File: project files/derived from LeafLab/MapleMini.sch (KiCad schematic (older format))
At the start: 39 parts

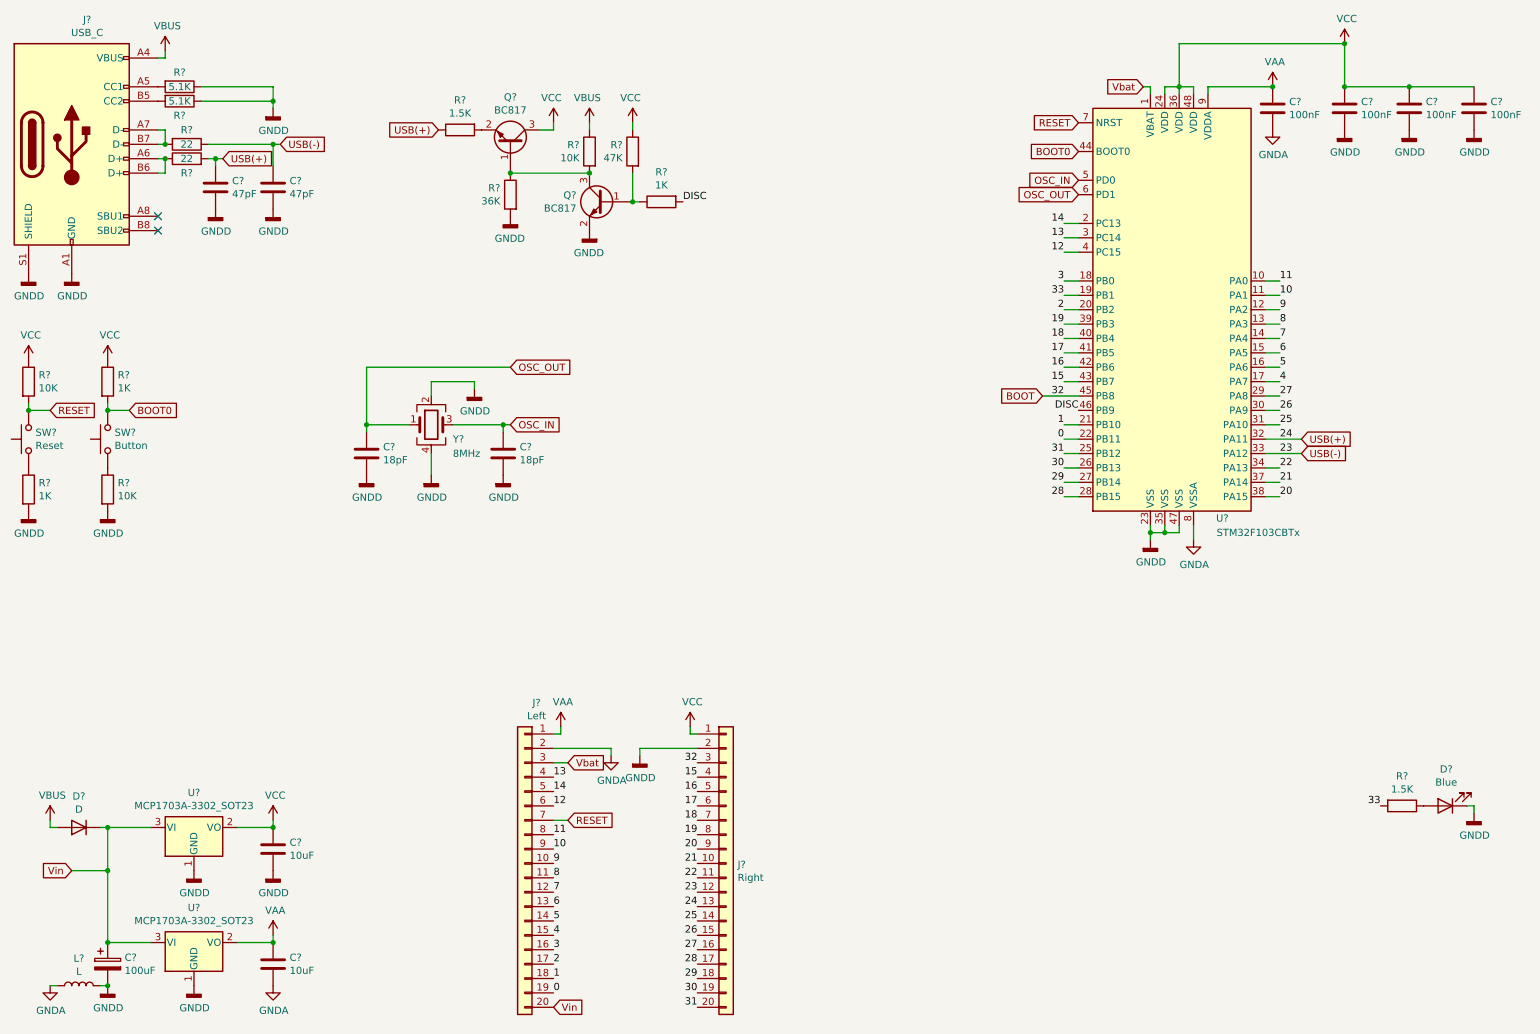
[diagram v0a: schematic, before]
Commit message: major re-arrangements
- Added references
- Added second schematic as derived from (supposengly) BAITE clone
- Renamed first design as LeafLabs-derived
- Added README.md
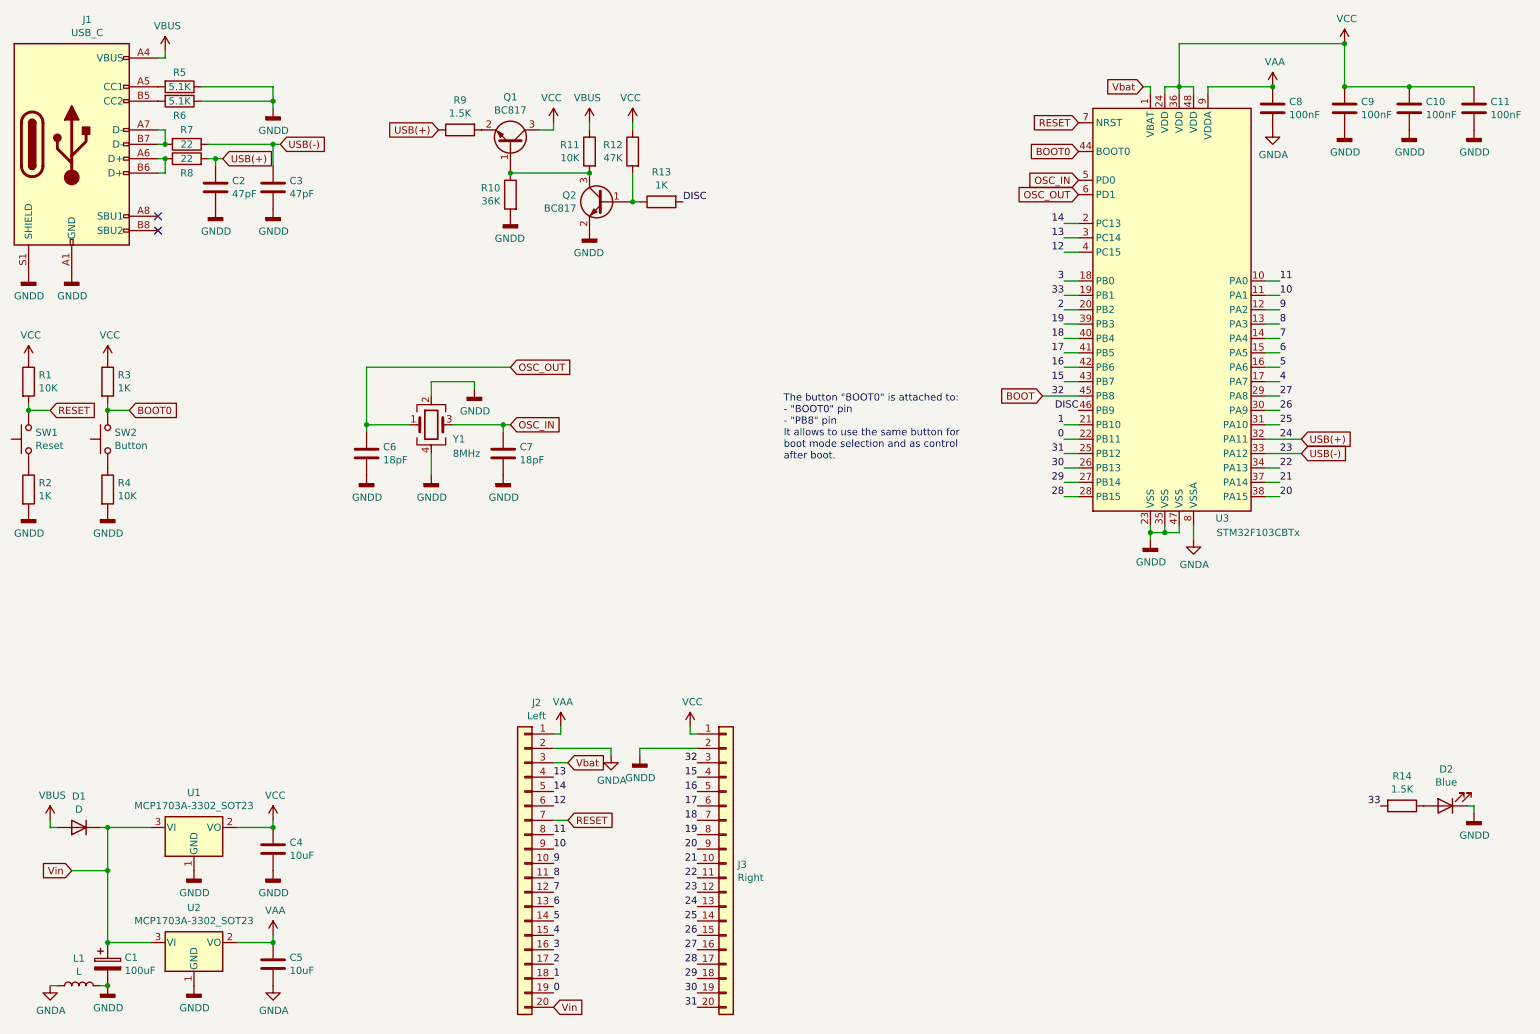
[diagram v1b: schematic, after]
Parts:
- C1, C10, C11, C2, C3, C4, C5, C6, C7, C8, C9: renamed from C?; footprint (none) -> Capacitor_SMD:C_0603_1608Metric
- D1: renamed from D?; footprint (none) -> Diode_SMD:D_SOD-323
- D2: renamed from D?; footprint (none) -> LED_SMD:LED_0805_2012Metric_Castellated
- J1: renamed from J?; footprint (none) -> Connector_USB:USB_C_Receptacle_Palconn_UTC16-G
- J2, J3: renamed from J?; footprint (none) -> Connector_PinHeader_2.54mm:PinHeader_1x20_P2.54mm_Vertical
- L1: renamed from L?; footprint (none) -> Inductor_SMD:L_0805_2012Metric
- R1, R10, R11, R12, R13, R14, R2, R3, R4, R5, R6, R7, R8, R9: renamed from R?; footprint (none) -> Resistor_SMD:R_0805_2012Metric
- SW1, SW2: renamed from SW?; footprint (none) -> Button_Switch_SMD:SW_SPST_B3U-1000P-B
- Y1: renamed from Y?; footprint (none) -> Crystal:Crystal_SMD_SeikoEpson_TSX3225-4Pin_3.2x2.5mm
- gave numbers to parts that had none: 5
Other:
- note added: "The button "BOOT0" is attached to:\n- "BOOT0" pin\n- "PB8" pin\nIt allows to use the same button for \nboot mode selection and as control\nafter boot."

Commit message: Coments on schematics
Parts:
- L1: value L -> 10uH
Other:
- note added: "Buttons and LED"
- note added: "Microcontroller core"
- note added: "Oscilator"
- note added: "Power Management"
- note added: "USB Type C as \nFull Speed USB 2.0"
- note added: "VCP control circuit"
- moved on the sheet: C10, C11, C2, C3, C6, C7, C8, C9, D2, J1, Q1, Q2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

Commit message: Diode search
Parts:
- D1: footprint Diode_SMD:D_SOD-323 -> Diode_SMD:D_SOD-123
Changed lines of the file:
@@
 F 0 "D1" H 1050 6083 50  0000 C CNN
 F 1 "D" H 1050 6174 50  0000 C CNN
-F 2 "Diode_SMD:D_SOD-323" H 1050 6300 50  0001 C CNN
+F 2 "Diode_SMD:D_SOD-123" H 1050 6300 50  0001 C CNN
 F 3 "~" H 1050 6300 50  0001 C CNN
 	1    1050 6300

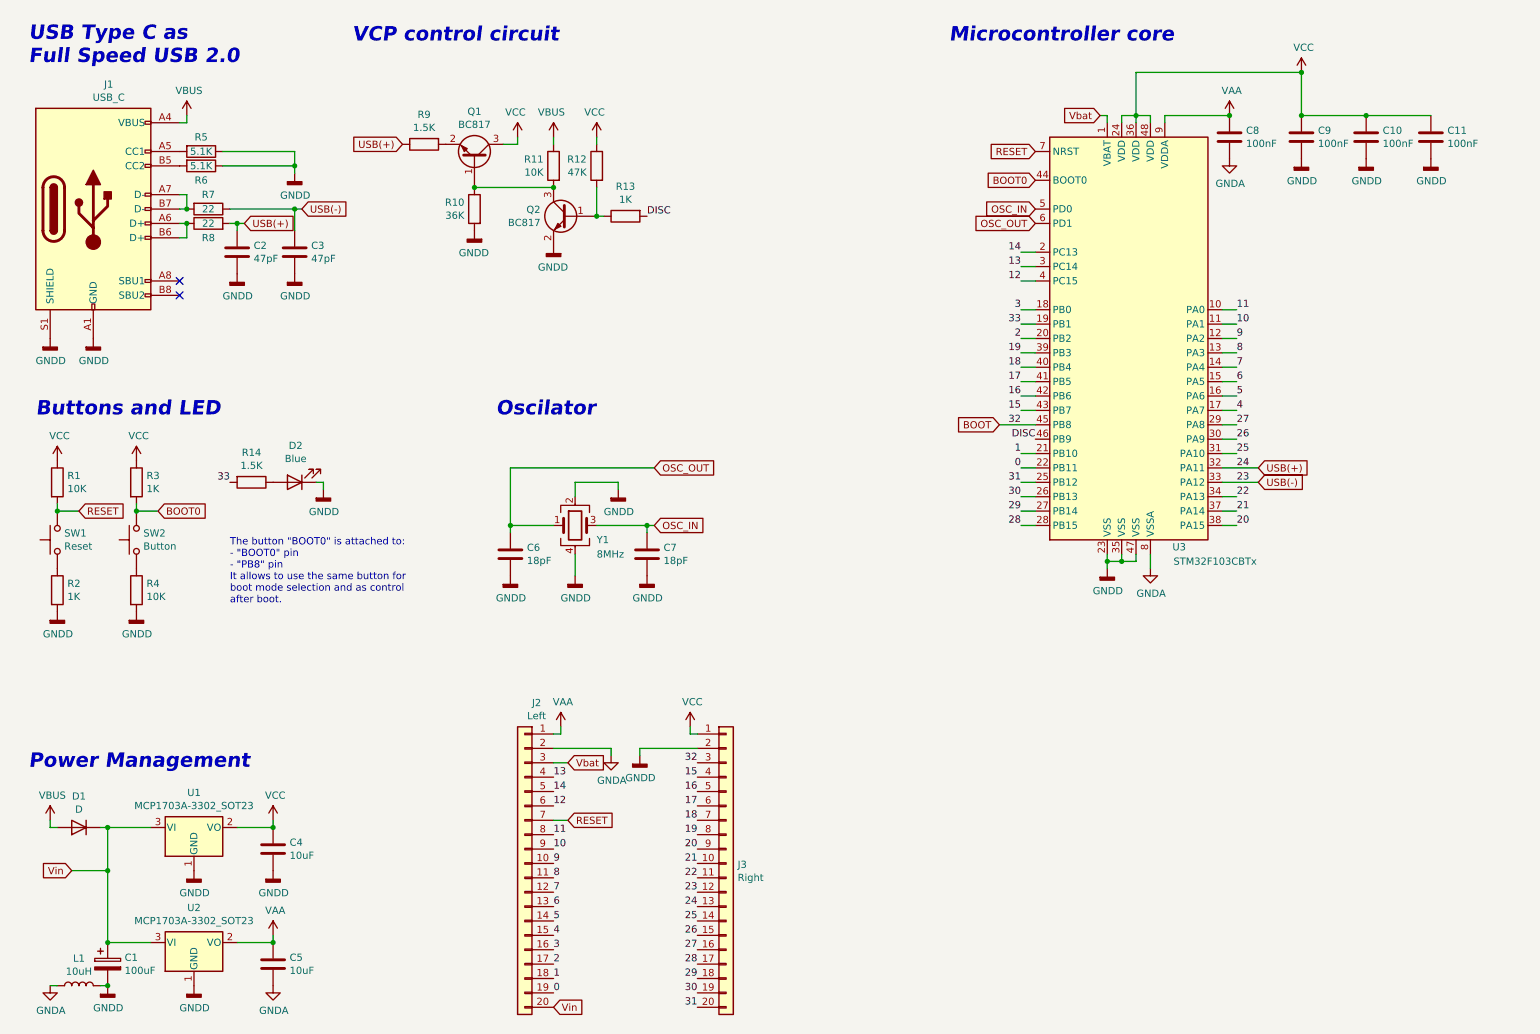
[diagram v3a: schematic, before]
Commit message: Added STDC connectors
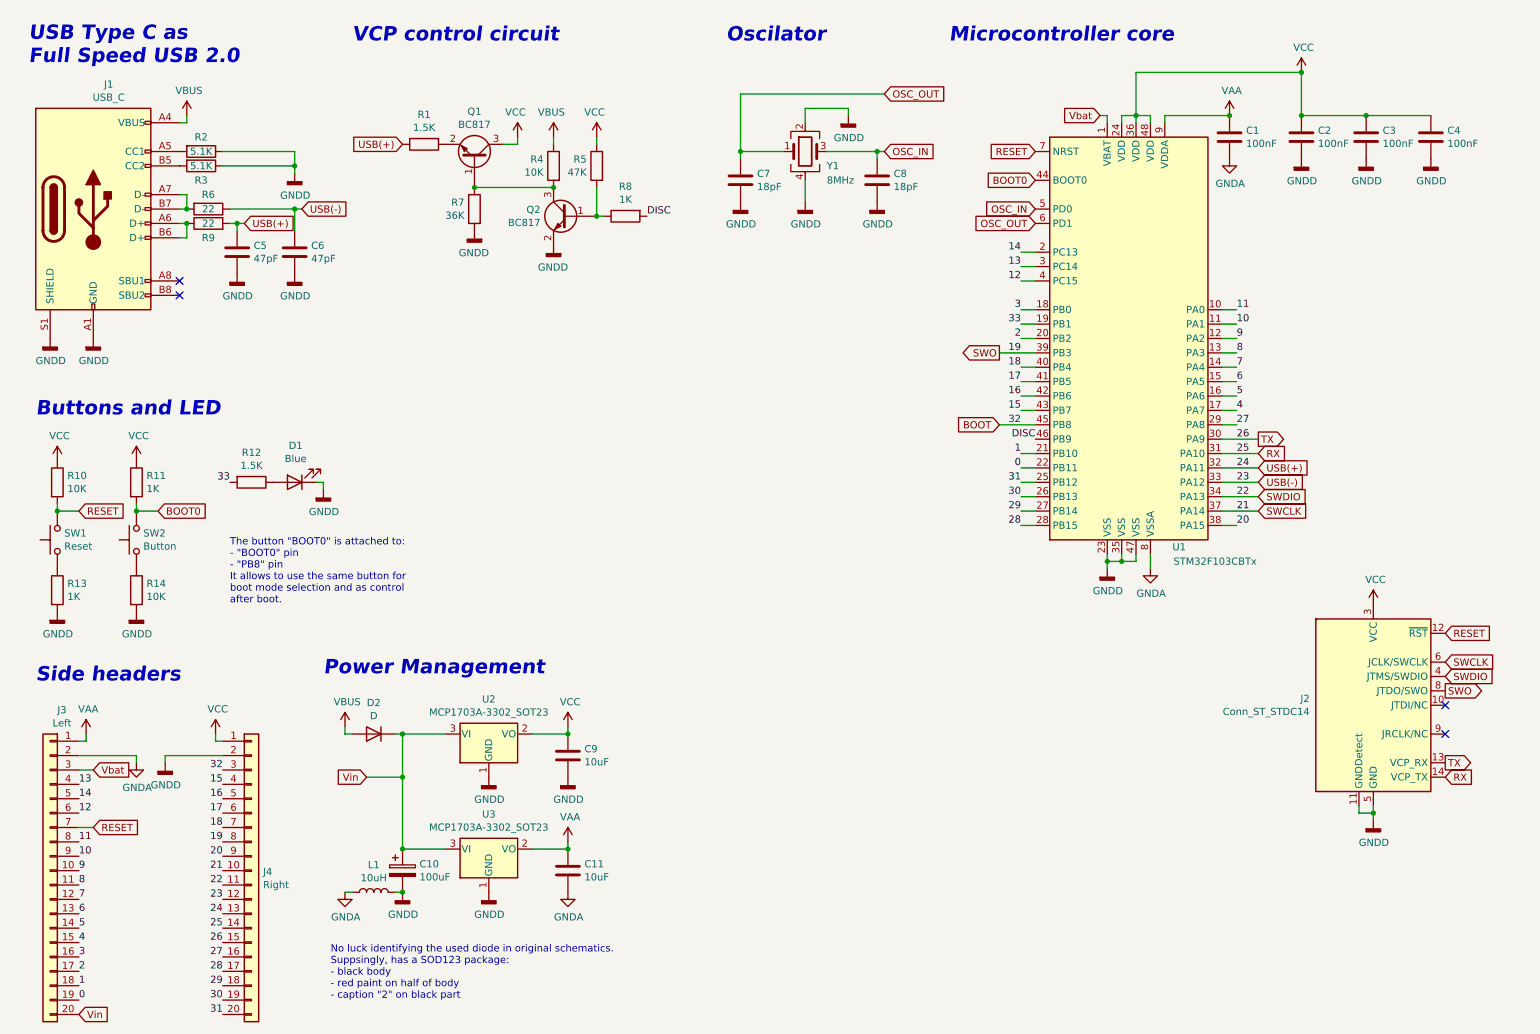
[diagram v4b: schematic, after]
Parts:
- added J2: Conn_ST_STDC14, Connector_PinHeader_1.27mm:PinHeader_2x07_P1.27mm_Vertical_SMD, symbol Connector:Conn_ST_STDC14
- renumbered C8 to C1, C1 to C10, C5 to C11, C9 to C2, C10 to C3, C11 to C4, C2 to C5, C3 to C6, C6 to C7, C7 to C8, C4 to C9, D2 to D1, D1 to D2, J2 to J3, J3 to J4, R9 to R1, R1 to R10, R3 to R11, R14 to R12, R2 to R13, R4 to R14, R5 to R2, R6 to R3, R11 to R4, R12 to R5, R7 to R6, R10 to R7, R13 to R8, R8 to R9, U3 to U1, U1 to U2, U2 to U3
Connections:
- net GNDD: now also J2.11 (GNDDetect), J2.5 (GND), J2.7 (GND)
- net RESET: now also J2.12 (~RST)
- net VCC: now also J2.3 (VCC)
- net 19 renamed SWO
- net SWO: now also J2.8 (JTDO/SWO)
- net 21 renamed SWCLK
- net SWCLK: now also J2.6 (JCLK/SWCLK)
- net 22 renamed SWDIO
- net SWDIO: now also J2.4 (JTMS/SWDIO)
- net 25 renamed RX
- net RX: now also J2.14 (VCP_TX)
- net 26 renamed TX
- net TX: now also J2.13 (VCP_RX)
- no-connect marks 2 -> 4
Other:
- note added: "No luck identifying the used diode in original schematics.\nSuppsingly, has a SOD123 package:\n- black body\n- red paint on half of body\n- caption "2" on black part"
- note added: "Side headers"
- moved on the sheet: C10, C11, C7, C8, C9, D2, J3, J4, L1, U2, U3, Y1
